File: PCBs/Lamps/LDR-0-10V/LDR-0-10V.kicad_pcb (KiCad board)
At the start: 2 copper layers, 40.6 x 33 mm, 11 parts, among them J1 POWER, J2 AO, U1 LM358

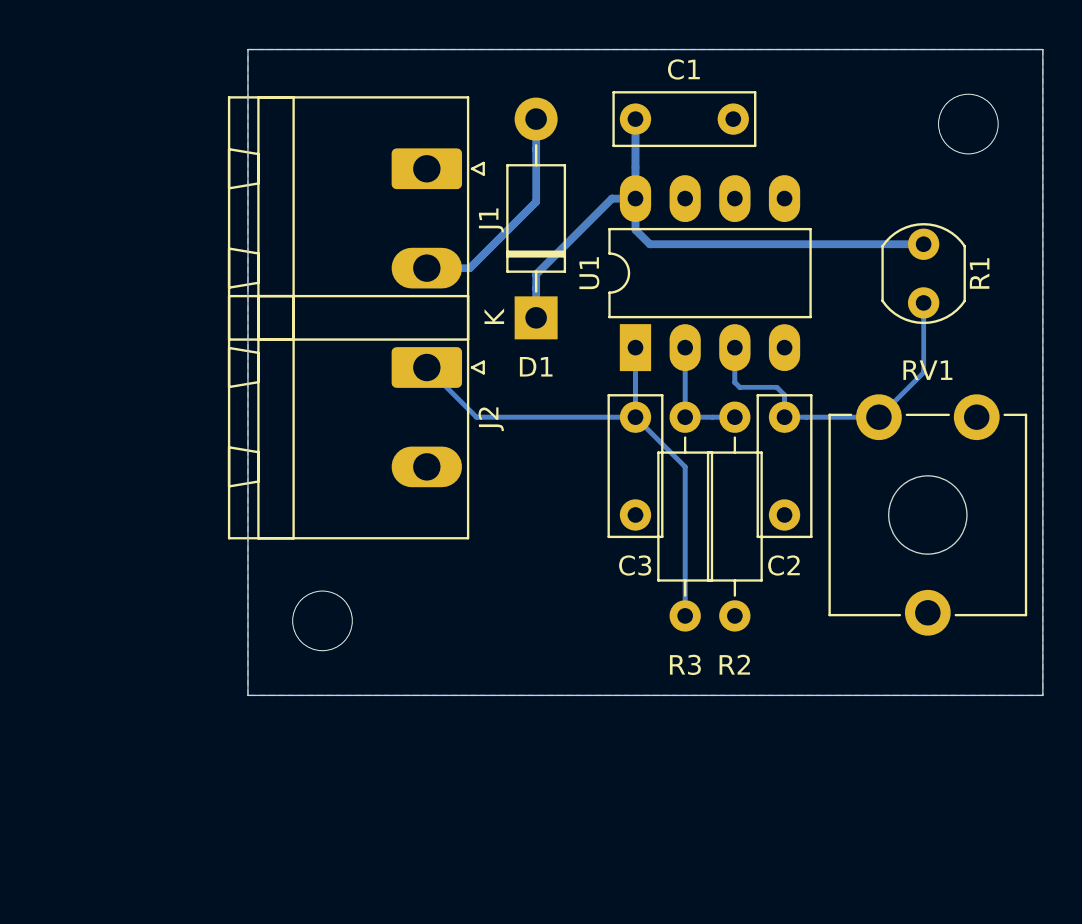
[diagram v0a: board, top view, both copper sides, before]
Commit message: General modification beacuse of dome light inflector
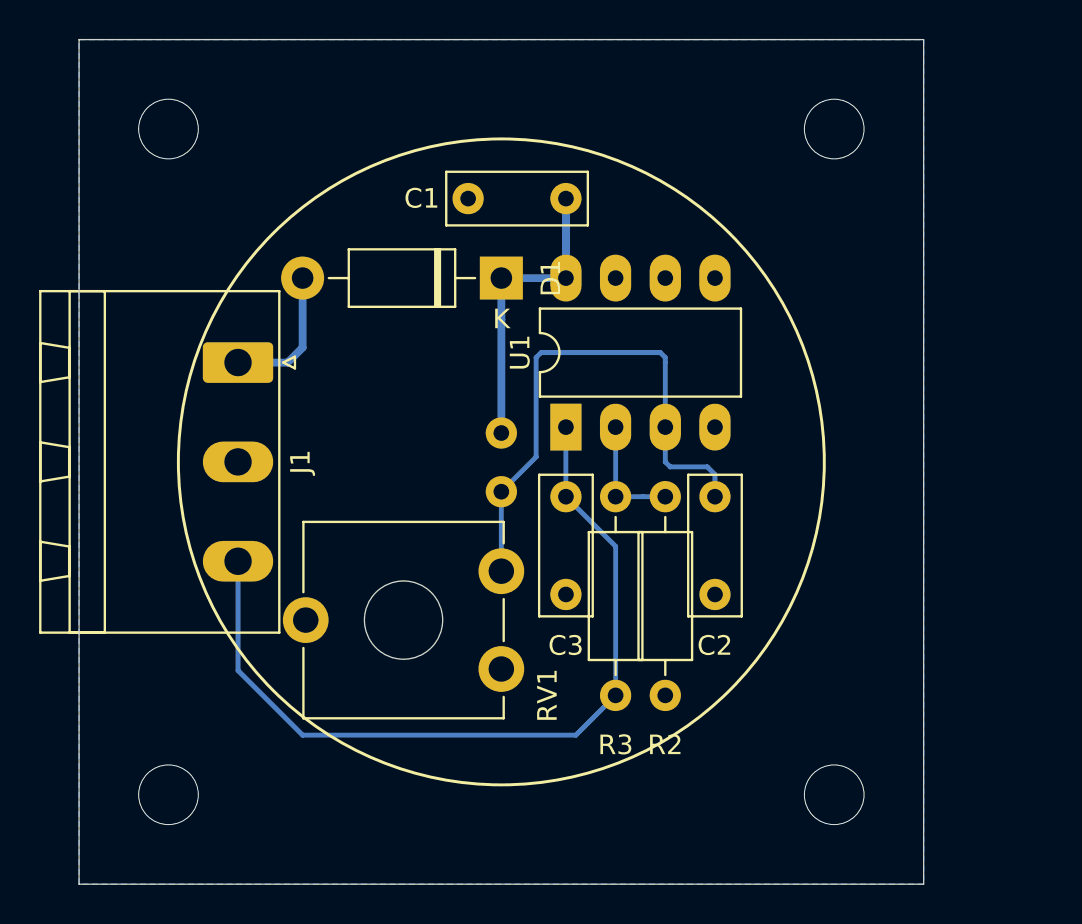
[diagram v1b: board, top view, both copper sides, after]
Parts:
- removed J2: AO, Connector_Phoenix_MSTB:PhoenixContact_MSTBA_2,5_2-G-5,08_1x02_P5.08mm_Horizontal
- J1: value POWER -> CON; footprint Connector_Phoenix_MSTB:PhoenixContact_MSTBA_2,5_2-G-5,08_1x02_P5.08mm_Horizontal -> Connector_Phoenix_MSTB:PhoenixContact_MSTBA_2,5_3-G-5,08_1x03_P5.08mm_Horizontal
- R1: moved to B.Cu
- moved R1 23.6 mm to (137.4, 95.8)
- moved RV1 20.8 mm to (137.4, 102.9), turned to 180 degrees
- moved J1 13.8 mm to (124.0, 92.2)
- moved R2 5.40 mm to (145.8, 109.2)
- moved R3 5.40 mm to (143.3, 109.2)
- moved C2 5.40 mm to (148.3, 99.1)
- moved C3 5.40 mm to (140.7, 99.1)
- moved U1 5.40 mm to (140.7, 95.5)
- moved C1 5.40 mm to (140.7, 83.8), turned to 180 degrees
- moved D1 2.70 mm to (137.4, 87.9), turned to 180 degrees
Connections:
- C3 pad 1: Net-(C3-Pad1) -> AO
- J1 pad 1: GND -> Net-(D1-Pad2)
- J1 pad 2: Net-(D1-Pad2) -> GND
- R3 pad 1: Net-(C3-Pad1) -> AO
- U1 pad 1: Net-(C3-Pad1) -> AO
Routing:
- net AO: track 0.00 -> 41.9 mm
- net Net-(C3-Pad1): track 26.5 -> 0.00 mm
- net VCC: track 29.6 -> 15.3 mm
- net Net-(C2-Pad1): track 17.3 -> 27.7 mm
- net Net-(D1-Pad2): track 11.2 -> 7.17 mm
- net (no net): vias 2 -> 4
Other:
- board size 40.6 x 33 mm -> 43.2 x 43.2 mm
